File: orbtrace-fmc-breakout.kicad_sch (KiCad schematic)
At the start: 34 parts, among them J1 Samtec_ASP-134604-01, J2 Conn_01x02, SW1 SW_SPST, SW2 SW_SPST, SW3 SW_SPST, SW4 SW_SPST, SW5 SW_DIP_x04

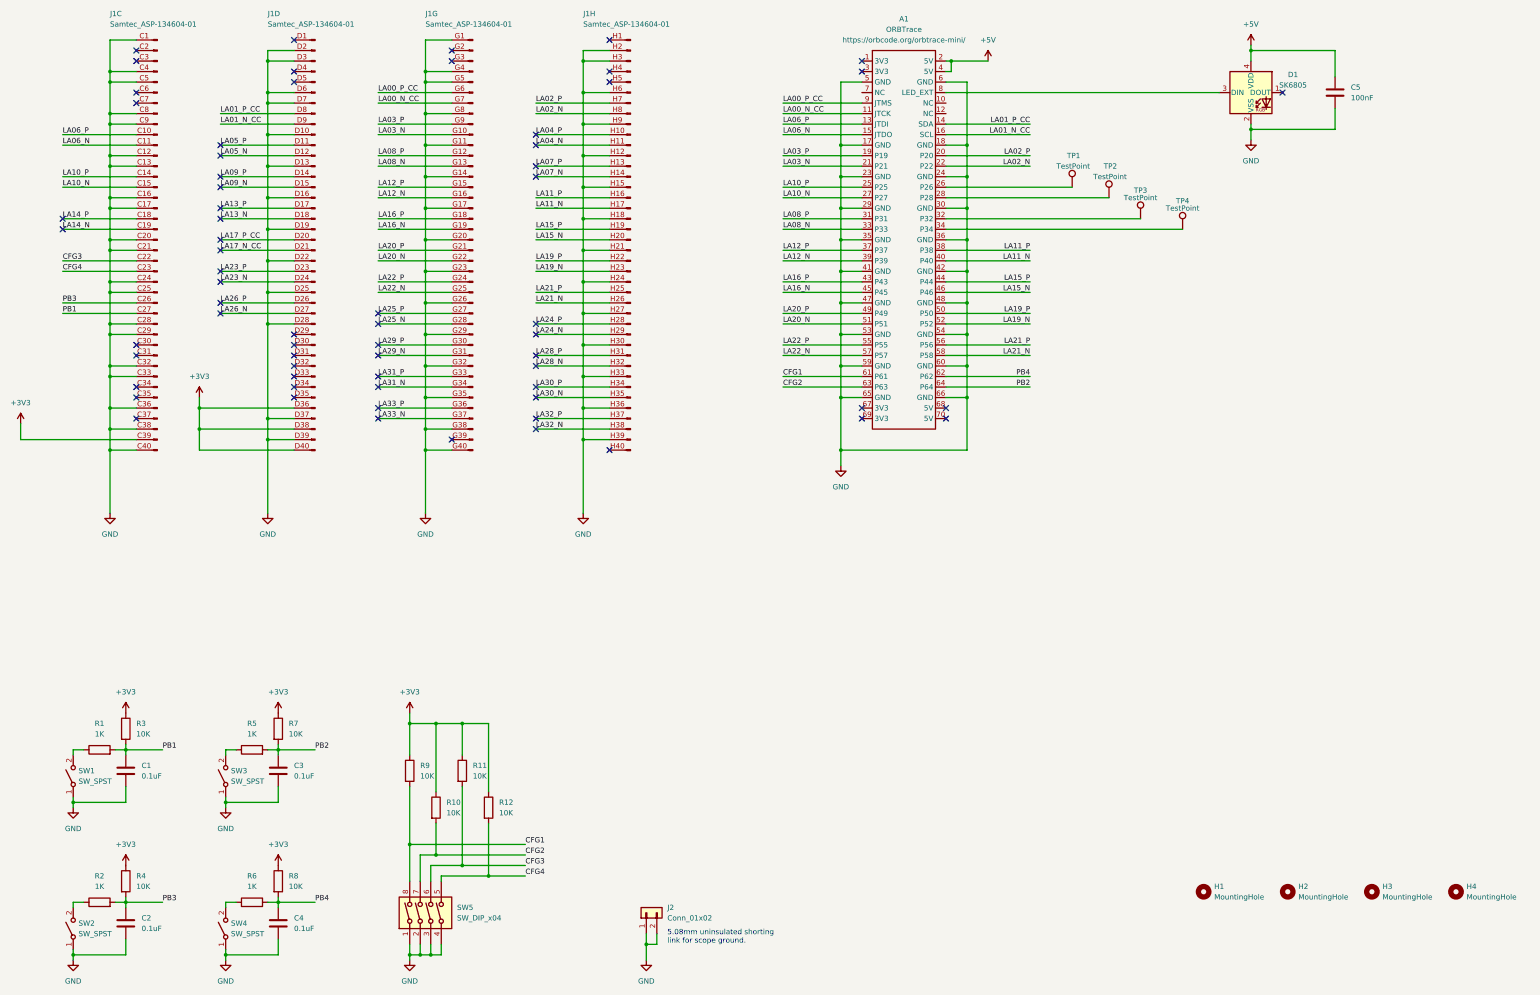
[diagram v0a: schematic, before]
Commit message: dev: fix for misaligned FMC
This commit fixes the FMC orientation by rotating it 180 degrees.  The
original layout was created while looking at a mirrored view of an
example FMC expansion board - oops.

This update also adds a standard 20-pin 0.1" pitch Arm debug connector
that is wired for SWD only.  In addition there are 2 8-pin 0.1" headers
connected to FPGA IO that can be used for user IO of any sort.
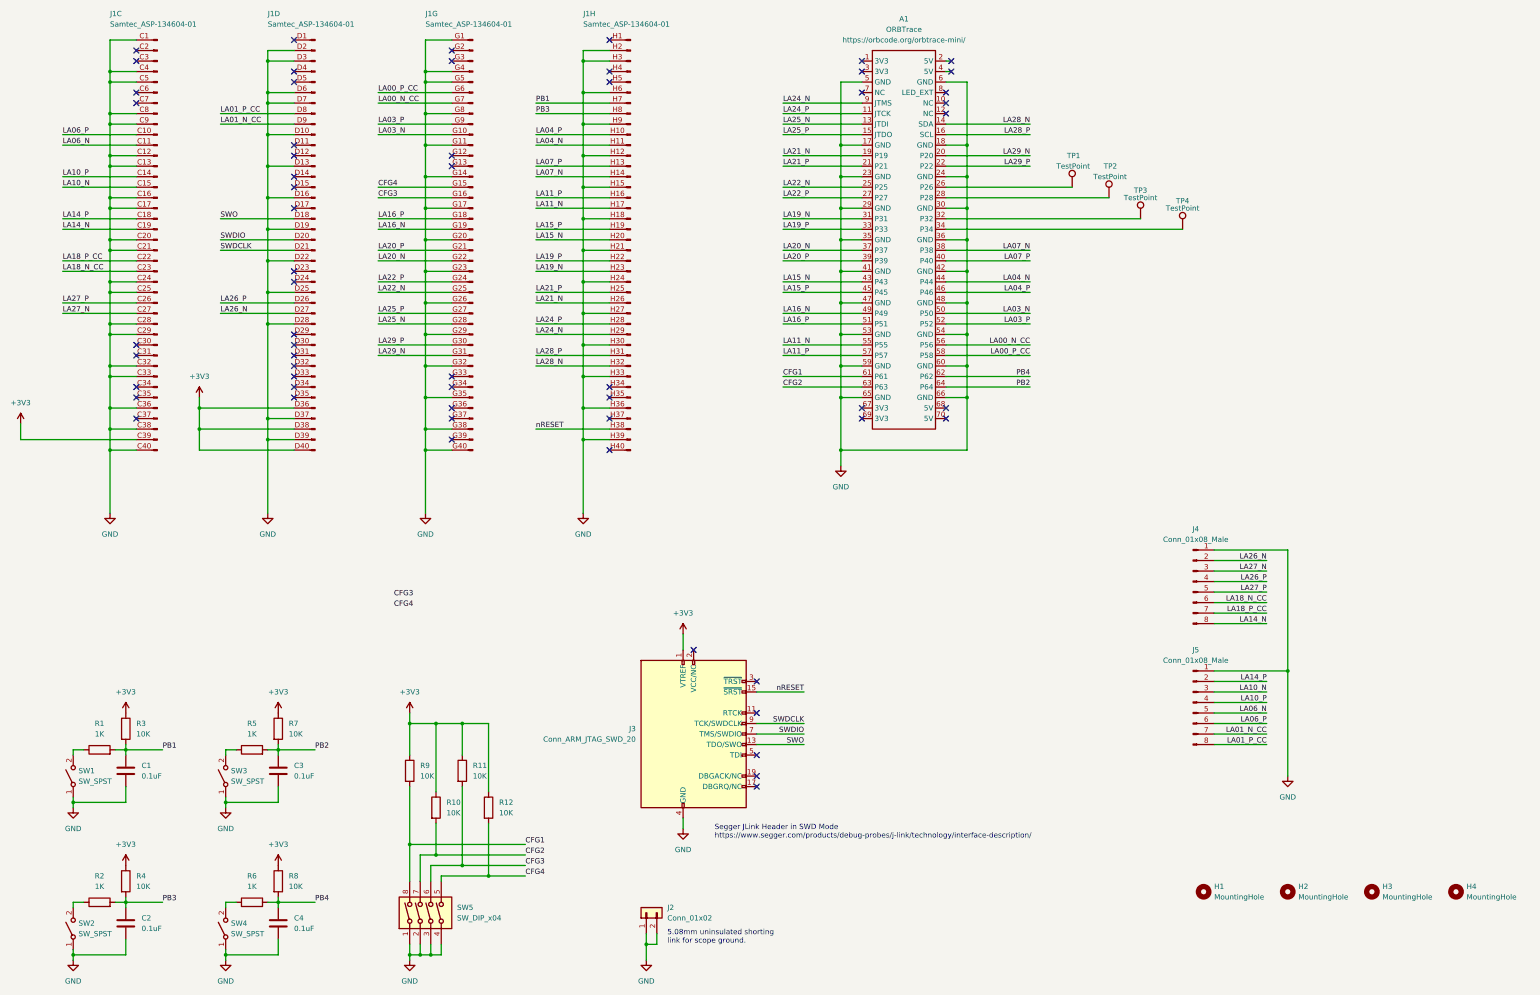
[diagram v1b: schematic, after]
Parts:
- removed C5: 100nF, Capacitor_SMD:C_0603_1608Metric, symbol Device:C
- removed D1: SK6805, LED_SMD:LED_SK6805_PLCC4_2.4x2.7mm_P1.3mm, symbol LED:SK6805
- added J3: Conn_ARM_JTAG_SWD_20, Connector_IDC:IDC-Header_2x10_P2.54mm_Vertical, symbol Connector:Conn_ARM_JTAG_SWD_20
- added J4, J5: Conn_01x08_Male, Connector_PinHeader_2.54mm:PinHeader_1x08_P2.54mm_Vertical, symbol Connector:Conn_01x08_Male
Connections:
- net +3V3: now also J3.1 (VTREF)
- net CFG3: now also J1.G16 (Pin_16); no longer J1.C22 (Pin_22)
- net CFG4: now also J1.G15 (Pin_15); no longer J1.C23 (Pin_23)
- net GND: now also J3.10 (GND), J3.12 (GND), J3.14 (GND), J3.16 (GND), J3.18 (GND), J3.20 (GND), J3.4 (GND), J3.6 (GND), J3.8 (GND), J4.1 (Pin_1), J5.1 (Pin_1)
- net LA00_N_CC: now also A1.56 (P56); no longer A1.11 (JTCK)
- net LA00_P_CC: now also A1.58 (P58); no longer A1.9 (JTMS)
- net LA01_N_CC: now also J5.7 (Pin_7); no longer A1.16 (SCL)
- net LA01_P_CC: now also J5.8 (Pin_8); no longer A1.14 (SDA)
- net LA03_N: now also A1.50 (P50); no longer A1.21 (P21)
- net LA03_P: now also A1.52 (P52); no longer A1.19 (P19)
- net LA04_N: now also A1.44 (P44)
- net LA04_P: now also A1.46 (P46)
- net LA06_N: now also J5.5 (Pin_5); no longer A1.15 (JTDO)
- net LA06_P: now also J5.6 (Pin_6); no longer A1.13 (JTDI)
- net LA07_N: now also A1.38 (P38)
- net LA07_P: now also A1.40 (P40)
- net LA10_N: now also J5.3 (Pin_3); no longer A1.27 (P27)
- net LA10_P: now also J5.4 (Pin_4); no longer A1.25 (P25)
- net LA11_N: now also A1.55 (P55); no longer A1.40 (P40)
- net LA11_P: now also A1.57 (P57); no longer A1.38 (P38)
- net LA14_N: now also J4.8 (Pin_8)
- net LA14_P: now also J5.2 (Pin_2)
- net LA15_N: now also A1.43 (P43); no longer A1.46 (P46)
- net LA15_P: now also A1.45 (P45); no longer A1.44 (P44)
- net LA16_N: now also A1.49 (P49); no longer A1.45 (P45)
- net LA16_P: now also A1.51 (P51); no longer A1.43 (P43)
- net LA19_N: now also A1.31 (P31); no longer A1.52 (P52)
- net LA19_P: now also A1.33 (P33); no longer A1.50 (P50)
- net LA20_N: now also A1.37 (P37); no longer A1.51 (P51)
- net LA20_P: now also A1.39 (P39); no longer A1.49 (P49)
- net LA21_N: now also A1.19 (P19); no longer A1.58 (P58)
- net LA21_P: now also A1.21 (P21); no longer A1.56 (P56)
- net LA22_N: now also A1.25 (P25); no longer A1.57 (P57)
- net LA22_P: now also A1.27 (P27); no longer A1.55 (P55)
- net LA24_N: now also A1.9 (JTMS)
- net LA24_P: now also A1.11 (JTCK)
- net LA25_N: now also A1.13 (JTDI)
- net LA25_P: now also A1.15 (JTDO)
- net LA26_N: now also J4.2 (Pin_2)
- net LA26_P: now also J4.4 (Pin_4)
- net LA28_N: now also A1.14 (SDA)
- net LA28_P: now also A1.16 (SCL)
- net LA29_N: now also A1.20 (P20)
- net LA29_P: now also A1.22 (P22)
- net PB1: now also J1.H7 (Pin_7); no longer J1.C27 (Pin_27)
- net PB3: now also J1.H8 (Pin_8); no longer J1.C26 (Pin_26)
- net +5V: no longer names the net of A1.2 (5V)
- net +5V: no longer A1.4 (5V)
- removed net LA02_N: A1.22 (P22), J1.H8 (Pin_8)
- removed net LA02_P: A1.20 (P20), J1.H7 (Pin_7)
- net LA05_N: no longer names the net of J1.D12 (Pin_12)
- net LA05_P: no longer names the net of J1.D11 (Pin_11)
- net LA08_N: no longer names the net of J1.G13 (Pin_13)
- net LA08_N: no longer A1.33 (P33)
- net LA08_P: no longer names the net of J1.G12 (Pin_12)
- net LA08_P: no longer A1.31 (P31)
- net LA09_N: no longer names the net of J1.D15 (Pin_15)
- net LA09_P: no longer names the net of J1.D14 (Pin_14)
- removed net LA12_N: A1.39 (P39), J1.G16 (Pin_16)
- removed net LA12_P: A1.37 (P37), J1.G15 (Pin_15)
- net LA13_N renamed SWO
- net SWO: now also J3.13 (TDO/SWO)
- net LA13_P: no longer names the net of J1.D17 (Pin_17)
- net LA17_N_CC renamed SWDCLK
- net SWDCLK: now also J3.9 (TCK/SWDCLK)
- net LA17_P_CC renamed SWDIO
- net SWDIO: now also J3.7 (TMS/SWDIO)
- net LA23_N: no longer names the net of J1.D24 (Pin_24)
- net LA23_P: no longer names the net of J1.D23 (Pin_23)
- net LA30_N: no longer names the net of J1.H35 (Pin_35)
- net LA30_P: no longer names the net of J1.H34 (Pin_34)
- net LA31_N: no longer names the net of J1.G34 (Pin_34)
- net LA31_P: no longer names the net of J1.G33 (Pin_33)
- net LA32_N renamed nRESET
- net nRESET: now also J3.15 (~{SRST})
- net LA32_P: no longer names the net of J1.H37 (Pin_37)
- net LA33_N: no longer names the net of J1.G37 (Pin_37)
- net LA33_P: no longer names the net of J1.G36 (Pin_36)
- new net LA18_N_CC: J1.C23 (Pin_23), J4.6 (Pin_6)
- new net LA18_P_CC: J1.C22 (Pin_22), J4.7 (Pin_7)
- new net LA27_N: J1.C27 (Pin_27), J4.3 (Pin_3)
- new net LA27_P: J1.C26 (Pin_26), J4.5 (Pin_5)
- no-connect marks 67 -> 60
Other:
- note added: "Segger JLink Header in SWD Mode https://www.segger.com/products/debug-probes/j-link/technology/interface-description/"
